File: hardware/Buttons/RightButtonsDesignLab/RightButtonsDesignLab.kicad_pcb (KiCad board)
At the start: 2 copper layers, 26 x 105 mm, 5 parts, among them J1 Conn_01x03, J2 Conn_01x01, SW1 SW_Push, SW2 SW_Push, SW3 SW_Push

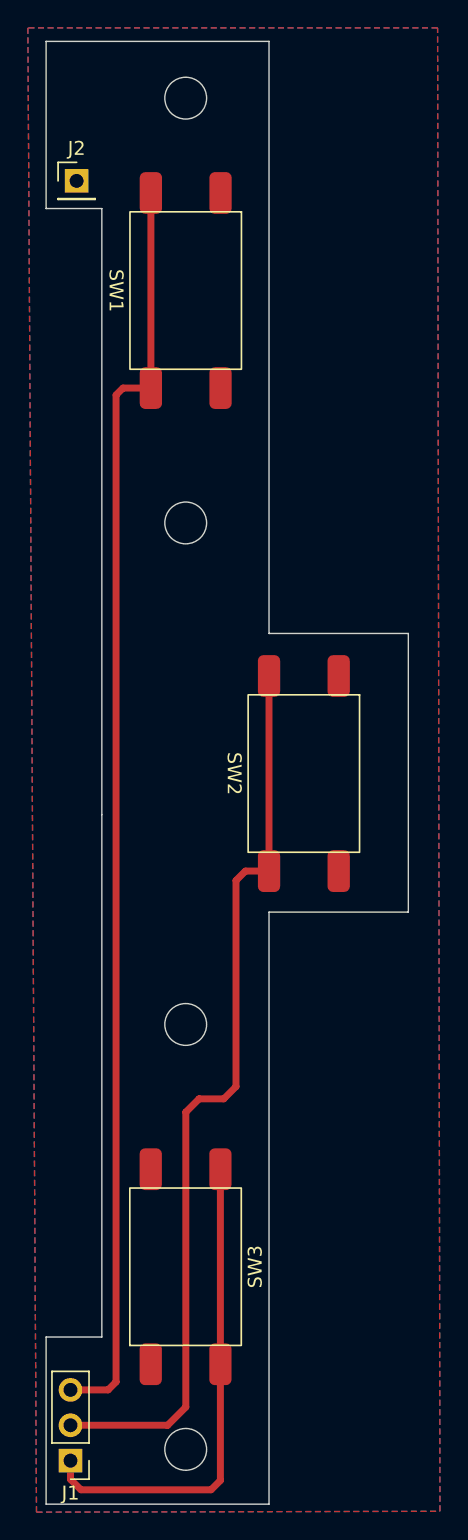
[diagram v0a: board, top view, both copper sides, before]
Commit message: update labels buttons
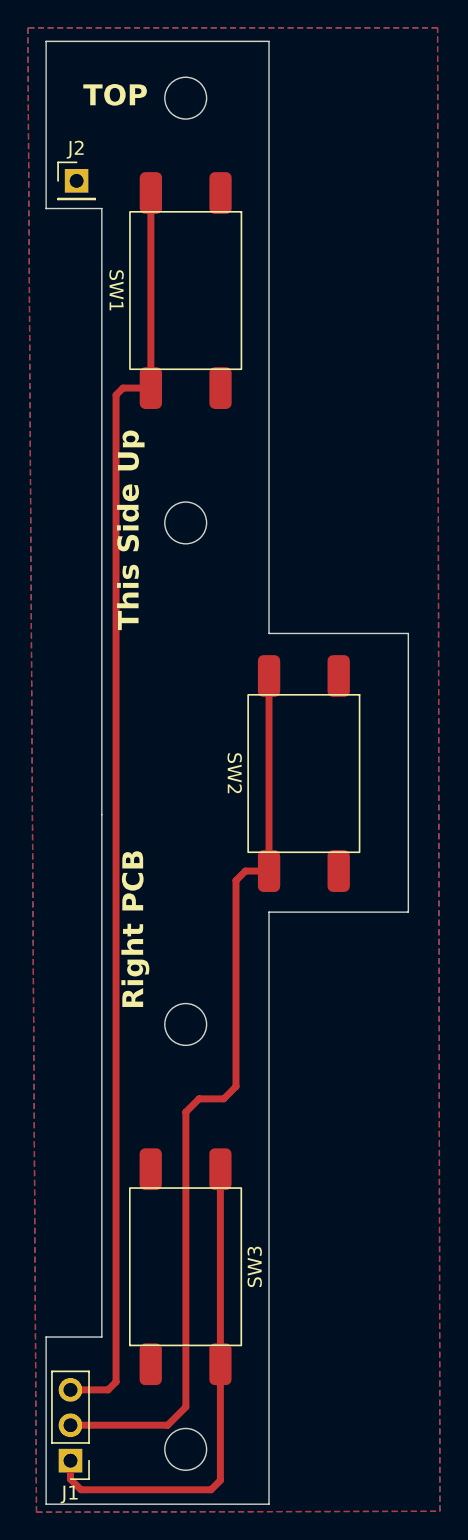
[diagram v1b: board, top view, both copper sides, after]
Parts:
- added G***: LOGO, LOGO, B.Cu at (131.7, 90.3)
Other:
- board text added: "Right PCB"
- board text added: "TOP"
- board text added: "This Side Up"

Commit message: Update labels
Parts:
- removed G***: LOGO, LOGO
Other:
- board text added: "This side up >"
- board text removed: "This Side Up"

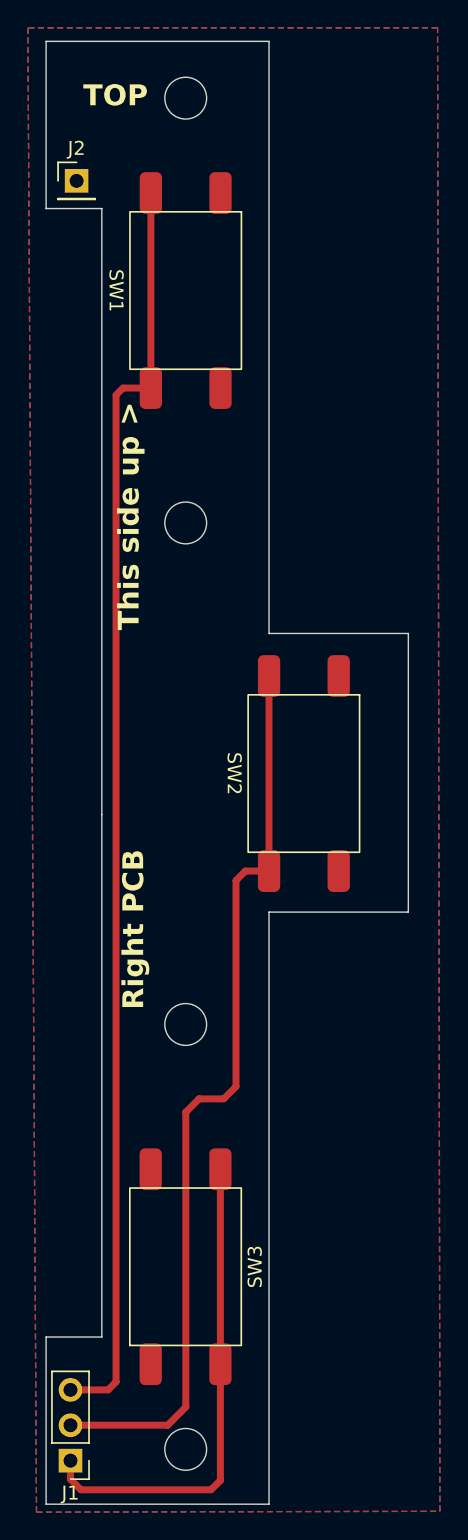
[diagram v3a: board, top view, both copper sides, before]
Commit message: SD, USB and labels changed
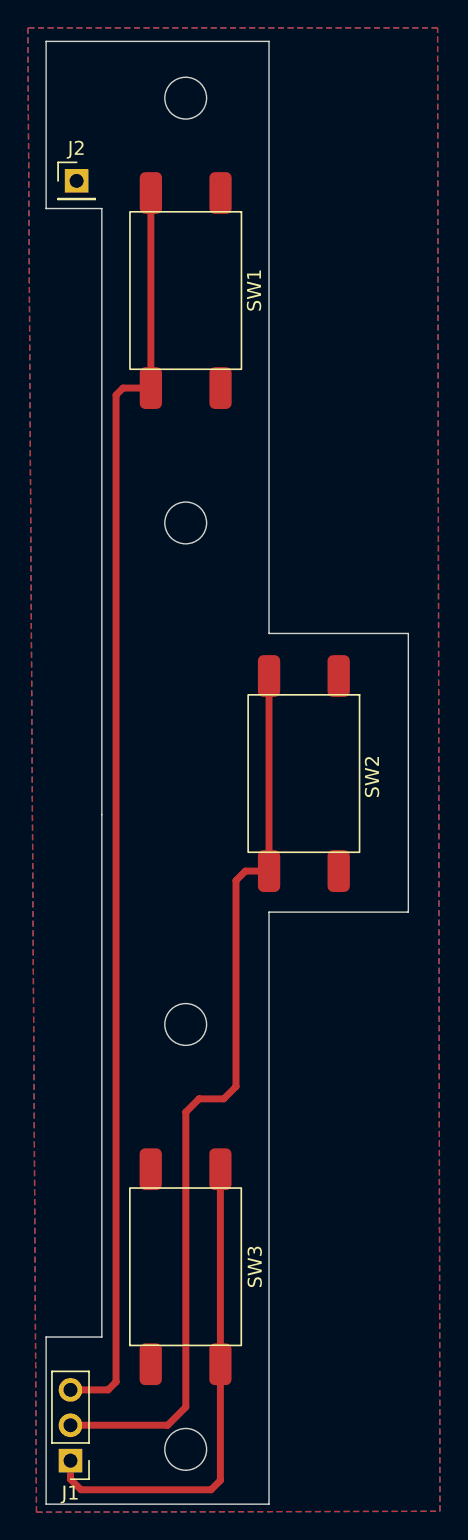
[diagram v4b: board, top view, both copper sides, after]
